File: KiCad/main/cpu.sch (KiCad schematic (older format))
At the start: 15 parts, among them SW1 SW_Push, U1 74HC245, U2 8284, U3 74HC245, U4 8086, U5 74HC573, U6 74HC573, U7 74HC573, Y1 30 MHz

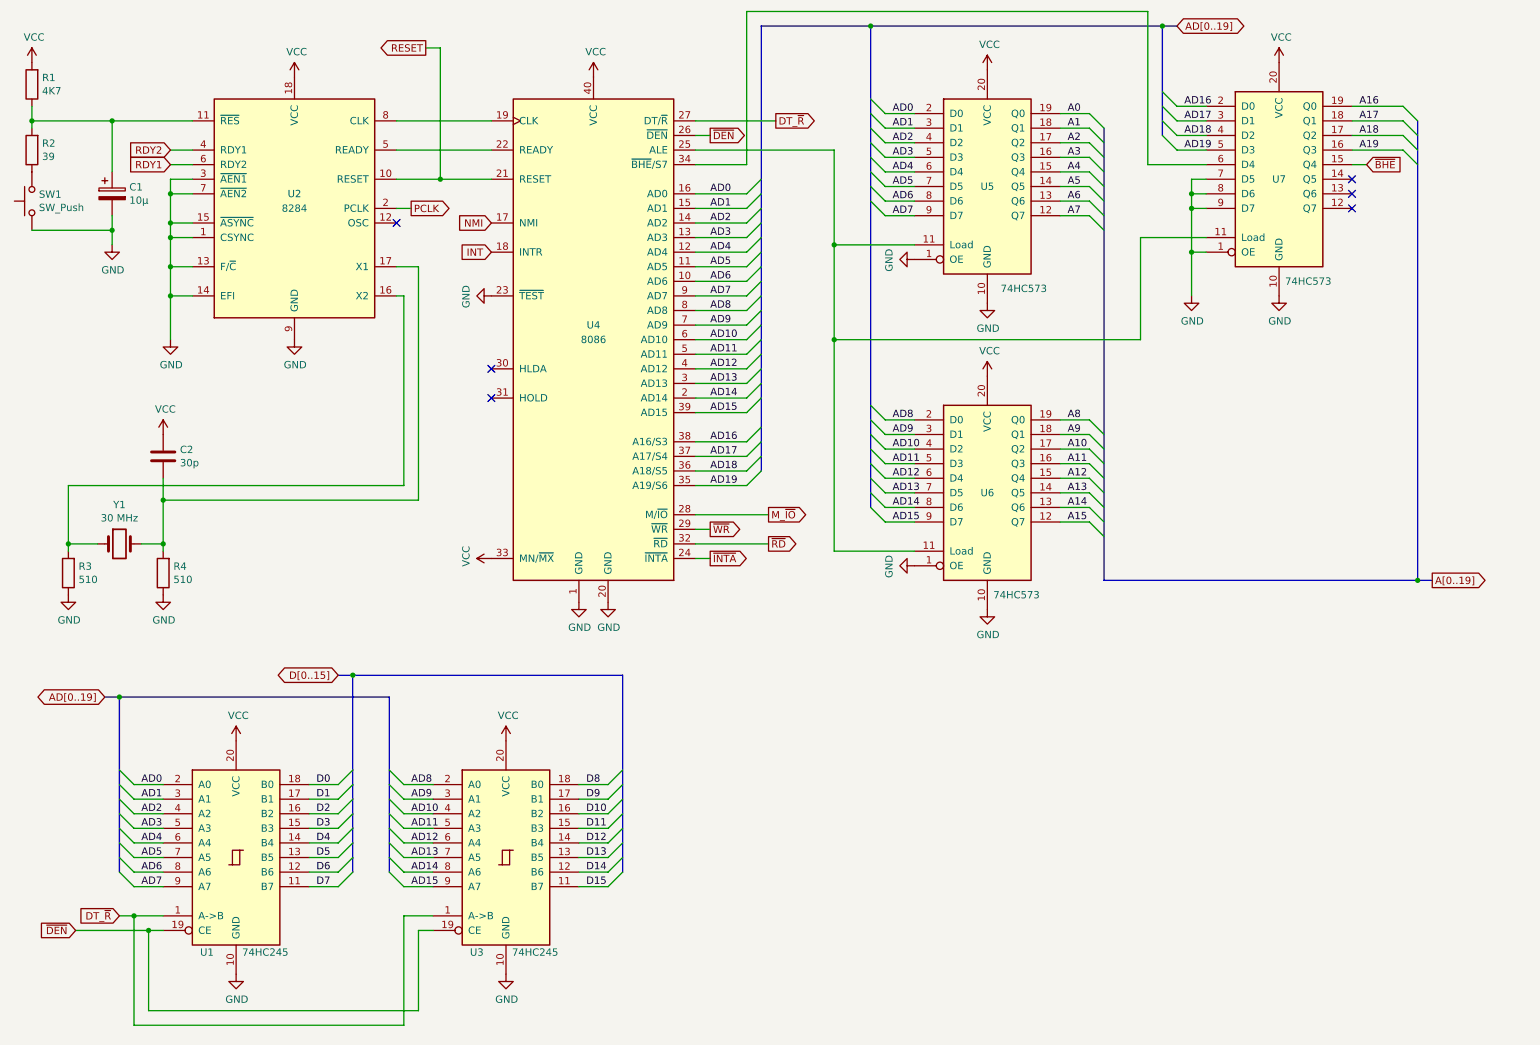
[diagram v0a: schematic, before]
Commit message: Updated graphics adapter and main schematics + board.
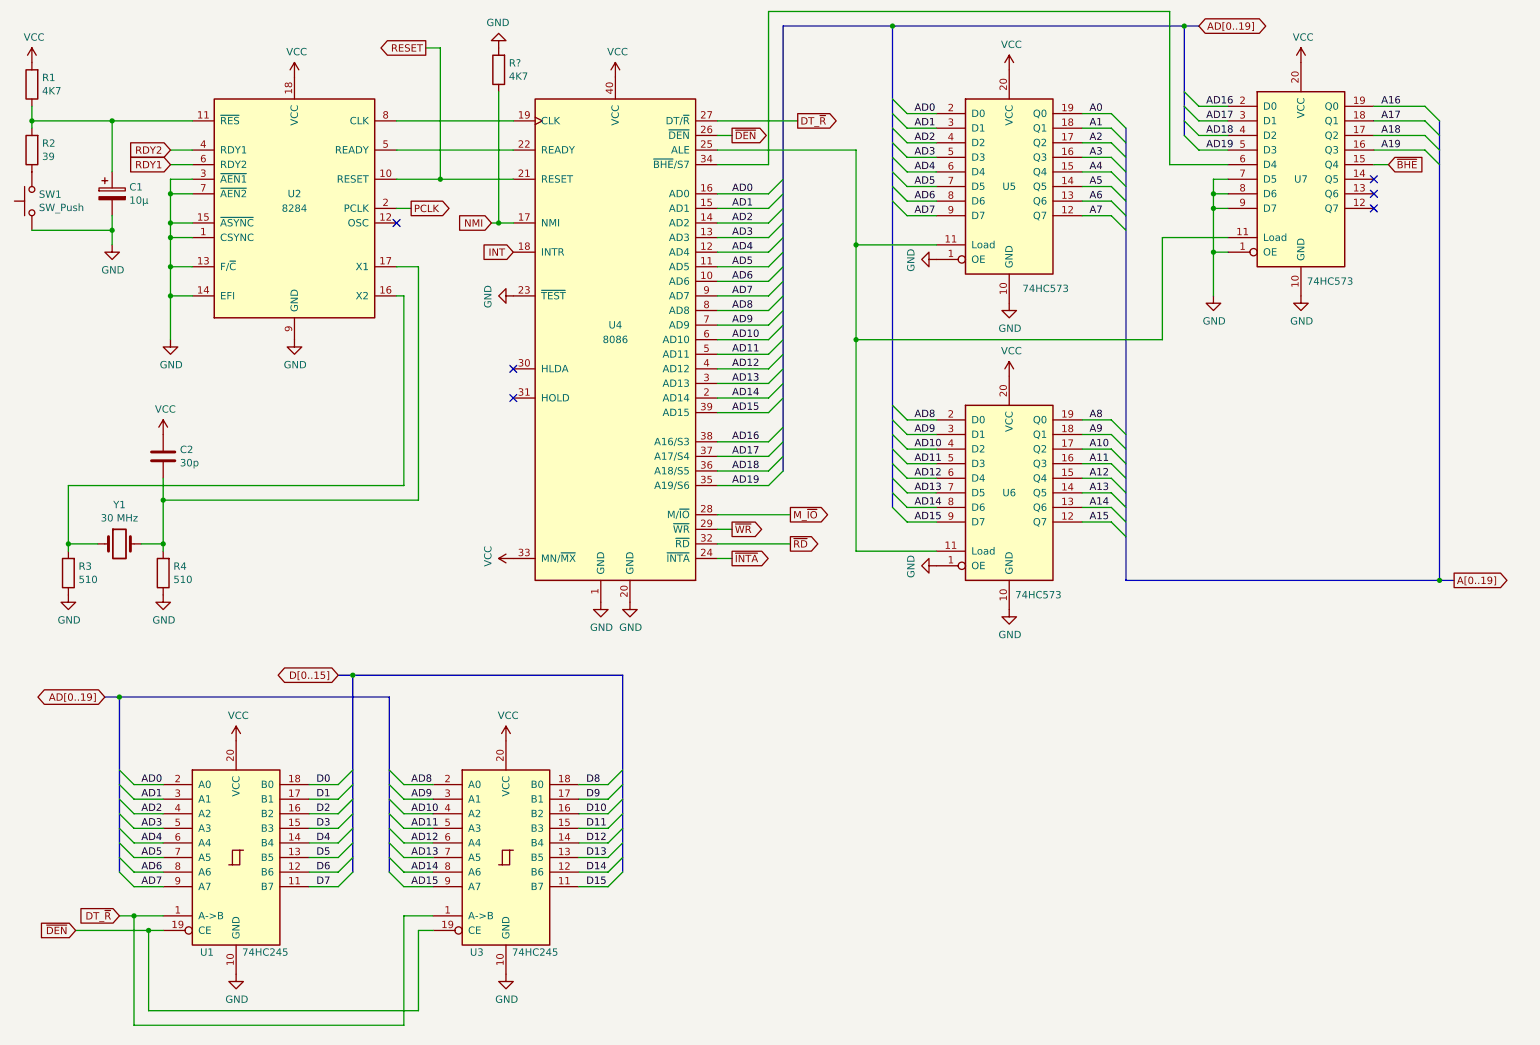
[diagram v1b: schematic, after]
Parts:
- added R?: 4K7, Resistor_THT:R_Axial_DIN0207_L6.3mm_D2.5mm_P7.62mm_Horizontal, symbol Device:R
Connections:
- net GND: now also R?.2
- net NMI: now also R?.1
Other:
- moved on the sheet: U4, U5, U6, U7

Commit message: Updated KiCad VGA board and main board.
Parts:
- added R7, R8: 4K7, Resistor_THT:R_Axial_DIN0207_L6.3mm_D2.5mm_P7.62mm_Horizontal, symbol Device:R
- gave numbers to parts that had none: 1
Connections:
- net GND: now also R7.1, R8.1; no longer U2.15 (~ASYNC~)
- net RDY1: now also R8.2
- net RDY2: now also R7.2
- no-connect marks 6 -> 8
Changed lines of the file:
@@
 	2050 1850 1900 1850
-Wire Wire Line
-	1900 1850 1900 2050
-Wire Wire Line
-	2050 2050 1900 2050
-Connection ~ 1900 2050
-Wire Wire Line
-	1900 2050 1900 2150
 Wire Wire Line
 	2050 1750 1900 1750
@@
 	4250 2050 4150 2050
 $Comp
-L Device:R R?
+L Device:R R6
 U 1 1 5F819246
 P 4150 1000
-F 0 "R?" H 4080 954 50  0000 R CNN
+F 0 "R6" H 4080 954 50  0000 R CNN
 F 1 "4K7" H 4080 1045 50  0000 R CNN
 F 2 "Resistor_THT:R_Axial_DIN0207_L6.3mm_D2.5mm_P7.62mm_Horizontal" V 4080 1000 50  0001 C CNN
@@
 	4150 2050 4100 2050
 $Comp
-L power:GND #PWR?
+L power:GND #PWR0102
 U 1 1 5F833B90
 P 4150 850
-F 0 "#PWR?" H 4150 600 50  0001 C CNN
+F 0 "#PWR0102" H 4150 600 50  0001 C CNN
 F 1 "GND" H 4155 677 50  0000 C CNN
 F 2 "" H 4150 850 50  0001 C CNN
@@
 	-1   0    0    1
 $EndComp
+Wire Wire Line
+	1900 1850 1900 2150
+NoConn ~ 2050 2050
+Text GLabel 5950 5450 1    50   Input ~ 0
+RDY2
+Text GLabel 6250 5450 1    50   Input ~ 0
+RDY1
+$Comp
+L Device:R R7
+U 1 1 5F82E30F
+P 5950 5700
+F 0 "R7" H 5880 5654 50  0000 R CNN
+F 1 "4K7" H 5880 5745 50  0000 R CNN
+F 2 "Resistor_THT:R_Axial_DIN0207_L6.3mm_D2.5mm_P7.62mm_Horizontal" V 5880 5700 50  0001 C CNN
+F 3 "~" H 5950 5700 50  0001 C CNN
+	1    5950 5700
+	-1   0    0    1
+$EndComp
+$Comp
+L power:GND #PWR056
+U 1 1 5F82EA67
+P 5950 6150
+F 0 "#PWR056" H 5950 5900 50  0001 C CNN
+F 1 "GND" H 5955 5977 50  0000 C CNN
+F 2 "" H 5950 6150 50  0001 C CNN
+F 3 "" H 5950 6150 50  0001 C CNN
+	1    5950 6150
+	1    0    0    -1
+$EndComp
+$Comp
+L Device:R R8
+U 1 1 5F82EE29
+P 6250 5700
+F 0 "R8" H 6180 5654 50  0000 R CNN
+F 1 "4K7" H 6180 5745 50  0000 R CNN
+F 2 "Resistor_THT:R_Axial_DIN0207_L6.3mm_D2.5mm_P7.62mm_Horizontal" V 6180 5700 50  0001 C CNN
+F 3 "~" H 6250 5700 50  0001 C CNN
+	1    6250 5700
+	-1   0    0    1
+$EndComp
+NoConn ~ 5150 4900
+Wire Wire Line
+	5950 5850 5950 6000
+Wire Wire Line
+	6250 5850 6250 6000
+Wire Wire Line
+	6250 6000 5950 6000
+Connection ~ 5950 6000
+Wire Wire Line
+	5950 6000 5950 6150
+Wire Wire Line
+	6250 5550 6250 5450
+Wire Wire Line
+	5950 5550 5950 5450
 Wire Bus Line
 	10600 1350 10600 4500

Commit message: Updated main system board schematics and board.
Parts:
- added U13: 74HC32, Package_DIP:DIP-14_W7.62mm_LongPads, symbol 74xx:74LS32
- added U15: 74HC08, Package_DIP:DIP-14_W7.62mm_LongPads, symbol 74xx:74LS08
- R7, R8: value 4K7 -> 10K
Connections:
- net A0: now also U15.1
- net GND: now also U15.10, U15.12, U15.13, U15.7 (GND), U15.9
- net RESET: now also U15.6; no longer U2.10 (RESET), U4.21 (RESET)
- net VCC: now also U15.14 (VCC)
- net ~BHE: now also U13.13
- net ~DEN: now also U13.12, U13.9; no longer U1.19 (CE), U3.19 (CE)
- net ~INTA: now also U15.2
- net CLK: now reaches U2.8 (CLK), U4.19 (CLK)
- net READY: now reaches U2.5 (READY), U4.22 (READY)
- net ALE: now reaches U4.25 (ALE), U5.11 (Load), U6.11 (Load), U7.11 (Load)
- net ~RES: now reaches C1.1, R1.1, R2.2, U2.11 (~RES~)
- new net: U13.10, U15.3
- new net CPU_RESET: U15.4, U15.5, U2.10 (RESET), U4.21 (RESET)
- new net ~CE_DHI: U13.11, U3.19 (CE)
- new net ~CE_DLO: U1.19 (CE), U13.8
- no-connect marks 8 -> 9
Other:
- moved on the sheet: R7, R8, U1, U3

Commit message: Fixed main and info_board bugs.
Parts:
- R7, R8: value 10K -> 4K7
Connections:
- net GND: now also U4.31 (HOLD); no longer R7.1, R8.1
- net VCC: now also R7.1, R8.1
- no-connect marks 9 -> 8
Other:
- moved on the sheet: R7, R8, U15C, U15D, U15E
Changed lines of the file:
@@
 A19
 Wire Wire Line
-	5200 7350 3350 7350
-NoConn ~ 4250 3250
+	5200 7350 3400 7350
 NoConn ~ 4250 3050
 NoConn ~ 3450 2050
-Text GLabel 1500 6700 0    50   Input ~ 0
+Text GLabel 1550 6700 0    50   Input ~ 0
 ~DEN
 Text GLabel 3250 6700 0    50   Input ~ 0
 DT_~R
-Connection ~ 3350 6700
-Wire Wire Line
-	3250 6700 3350 6700
-Wire Wire Line
-	3350 6700 3550 6700
-Wire Wire Line
-	3350 7350 3350 6700
+Connection ~ 3400 6700
+Wire Wire Line
+	3250 6700 3400 6700
+Wire Wire Line
+	3400 6700 3550 6700
+Wire Wire Line
+	3400 7350 3400 6700
 Wire Wire Line
 	5200 6700 5200 7350
@@
 	1900 1850 1900 2150
 NoConn ~ 2050 2050
-Text GLabel 9150 3250 1    50   Input ~ 0
+Text GLabel 9550 3950 3    50   Input ~ 0
 RDY2
-Text GLabel 9450 3250 1    50   Input ~ 0
+Text GLabel 9250 3950 3    50   Input ~ 0
 RDY1
 $Comp
 L Device:R R7
 U 1 1 5F82E30F
-P 9150 3500
-F 0 "R7" H 9080 3454 50  0000 R CNN
-F 1 "10K" H 9080 3545 50  0000 R CNN
-F 2 "Resistor_THT:R_Axial_DIN0207_L6.3mm_D2.5mm_P7.62mm_Horizontal" V 9080 3500 50  0001 C CNN
-F 3 "~" H 9150 3500 50  0001 C CNN
-	1    9150 3500
-	-1   0    0    1
-$EndComp
-$Comp
-L power:GND #PWR056
-U 1 1 5F82EA67
-P 9150 3950
-F 0 "#PWR056" H 9150 3700 50  0001 C CNN
-F 1 "GND" H 9155 3777 50  0000 C CNN
-F 2 "" H 9150 3950 50  0001 C CNN
-F 3 "" H 9150 3950 50  0001 C CNN
-	1    9150 3950
+P 9550 3700
+F 0 "R7" H 9480 3654 50  0000 R CNN
+F 1 "4K7" H 9480 3745 50  0000 R CNN
+F 2 "Resistor_THT:R_Axial_DIN0207_L6.3mm_D2.5mm_P7.62mm_Horizontal" V 9480 3700 50  0001 C CNN
+F 3 "~" H 9550 3700 50  0001 C CNN
+	1    9550 3700
 	1    0    0    -1
 $EndComp
@@
 L Device:R R8
 U 1 1 5F82EE29
-P 9450 3500
-F 0 "R8" H 9380 3454 50  0000 R CNN
-F 1 "10K" H 9380 3545 50  0000 R CNN
-F 2 "Resistor_THT:R_Axial_DIN0207_L6.3mm_D2.5mm_P7.62mm_Horizontal" V 9380 3500 50  0001 C CNN
-F 3 "~" H 9450 3500 50  0001 C CNN
-	1    9450 3500
-	-1   0    0    1
-$EndComp
-Wire Wire Line
-	9150 3650 9150 3800
-Wire Wire Line
-	9450 3650 9450 3800
-Wire Wire Line
-	9450 3800 9150 3800
-Connection ~ 9150 3800
-Wire Wire Line
-	9150 3800 9150 3950
-Wire Wire Line
-	9450 3350 9450 3250
-Wire Wire Line
-	9150 3350 9150 3250
+P 9250 3700
+F 0 "R8" H 9180 3654 50  0000 R CNN
+F 1 "4K7" H 9180 3745 50  0000 R CNN
+F 2 "Resistor_THT:R_Axial_DIN0207_L6.3mm_D2.5mm_P7.62mm_Horizontal" V 9180 3700 50  0001 C CNN
+F 3 "~" H 9250 3700 50  0001 C CNN
+	1    9250 3700
+	1    0    0    -1
+$EndComp
+Wire Wire Line
+	9550 3550 9550 3400
+Wire Wire Line
+	9250 3550 9250 3400
+Wire Wire Line
+	9250 3400 9550 3400
+Connection ~ 9550 3400
+Wire Wire Line
+	9550 3400 9550 3250
+Wire Wire Line
+	9250 3850 9250 3950
+Wire Wire Line
+	9550 3850 9550 3950
 Text Label 6250 1550 0    50   ~ 0
 ALE
@@
 ~CE_DHI
 Wire Wire Line
-	1500 6700 1700 6700
+	1550 6700 1700 6700
 Wire Wire Line
 	1850 7350 1700 7350
@@
 	1    0    0    -1
 $EndComp
-NoConn ~ 9350 5750
-NoConn ~ 9350 5100
-Wire Wire Line
-	8650 5000 8750 5000
-Wire Wire Line
-	8750 5200 8650 5200
-Connection ~ 8650 5200
-Wire Wire Line
-	8650 5200 8650 5000
-Wire Wire Line
-	8750 5850 8650 5850
-Wire Wire Line
-	8750 5650 8650 5650
-Connection ~ 8650 5650
-Wire Wire Line
-	8650 5650 8650 5200
-Wire Wire Line
-	8650 5650 8650 5850
-Connection ~ 8650 5850
+NoConn ~ 9350 5850
+NoConn ~ 9350 5200
+Wire Wire Line
+	8650 5100 8750 5100
+Wire Wire Line
+	8750 5300 8650 5300
+Connection ~ 8650 5300
+Wire Wire Line
+	8650 5300 8650 5100
+Wire Wire Line
+	8750 5950 8650 5950
+Wire Wire Line
+	8750 5750 8650 5750
+Connection ~ 8650 5750
+Wire Wire Line
+	8650 5750 8650 5300
+Wire Wire Line
+	8650 5750 8650 5950
+Connection ~ 8650 5950
 $Comp
 L power:GND #PWR0105
 U 1 1 5FA31EF9
-P 10100 6000
-F 0 "#PWR0105" H 10100 5750 50  0001 C CNN
-F 1 "GND" H 10105 5827 50  0000 C CNN
-F 2 "" H 10100 6000 50  0001 C CNN
-F 3 "" H 10100 6000 50  0001 C CNN
-	1    10100 6000
+P 10100 6100
+F 0 "#PWR0105" H 10100 5850 50  0001 C CNN
+F 1 "GND" H 10105 5927 50  0000 C CNN
+F 2 "" H 10100 6100 50  0001 C CNN
+F 3 "" H 10100 6100 50  0001 C CNN
+	1    10100 6100
 	1    0    0    -1
 $EndComp
@@
 L power:VCC #PWR0108
 U 1 1 5FA326F1
-P 10100 5000
-F 0 "#PWR0108" H 10100 4850 50  0001 C CNN
-F 1 "VCC" H 10115 5173 50  0000 C CNN
-F 2 "" H 10100 5000 50  0001 C CNN
-F 3 "" H 10100 5000 50  0001 C CNN
-	1    10100 5000
+P 10100 5100
+F 0 "#PWR0108" H 10100 4950 50  0001 C CNN
+F 1 "VCC" H 10115 5273 50  0000 C CNN
+F 2 "" H 10100 5100 50  0001 C CNN
+F 3 "" H 10100 5100 50  0001 C CNN
+	1    10100 5100
 	1    0    0    -1
 $EndComp
@@
 L 74xx:74LS08 U15
 U 3 1 5F933B11
-P 9050 5100
-F 0 "U15" H 9050 5425 50  0000 C CNN
-F 1 "74HC08" H 9050 5334 50  0000 C CNN
-F 2 "Package_DIP:DIP-14_W7.62mm_LongPads" H 9050 5100 50  0001 C CNN
-F 3 "http://www.ti.com/lit/gpn/sn74LS08" H 9050 5100 50  0001 C CNN
-	3    9050 5100
+P 9050 5200
+F 0 "U15" H 9050 5525 50  0000 C CNN
+F 1 "74HC08" H 9050 5434 50  0000 C CNN
+F 2 "Package_DIP:DIP-14_W7.62mm_LongPads" H 9050 5200 50  0001 C CNN
+F 3 "http://www.ti.com/lit/gpn/sn74LS08" H 9050 5200 50  0001 C CNN
+	3    9050 5200
 	1    0    0    -1
 $EndComp
@@
 L 74xx:74LS08 U15
 U 4 1 5F9359D8
-P 9050 5750
-F 0 "U15" H 9050 6075 50  0000 C CNN
-F 1 "74HC08" H 9050 5984 50  0000 C CNN
-F 2 "Package_DIP:DIP-14_W7.62mm_LongPads" H 9050 5750 50  0001 C CNN
-F 3 "http://www.ti.com/lit/gpn/sn74LS08" H 9050 5750 50  0001 C CNN
-	4    9050 5750
+P 9050 5850
+F 0 "U15" H 9050 6175 50  0000 C CNN
+F 1 "74HC08" H 9050 6084 50  0000 C CNN
+F 2 "Package_DIP:DIP-14_W7.62mm_LongPads" H 9050 5850 50  0001 C CNN
+F 3 "http://www.ti.com/lit/gpn/sn74LS08" H 9050 5850 50  0001 C CNN
+	4    9050 5850
 	1    0    0    -1
 $EndComp
@@
 L 74xx:74LS08 U15
 U 5 1 5F93755C
-P 10100 5500
-F 0 "U15" H 10330 5546 50  0000 L CNN
-F 1 "74HC08" H 10330 5455 50  0000 L CNN
-F 2 "Package_DIP:DIP-14_W7.62mm_LongPads" H 10100 5500 50  0001 C CNN
-F 3 "http://www.ti.com/lit/gpn/sn74LS08" H 10100 5500 50  0001 C CNN
-	5    10100 5500
-	1    0    0    -1
-$EndComp
-Wire Wire Line
-	8650 5850 8650 6100
+P 10100 5600
+F 0 "U15" H 10330 5646 50  0000 L CNN
+F 1 "74HC08" H 10330 5555 50  0000 L CNN
+F 2 "Package_DIP:DIP-14_W7.62mm_LongPads" H 10100 5600 50  0001 C CNN
+F 3 "http://www.ti.com/lit/gpn/sn74LS08" H 10100 5600 50  0001 C CNN
+	5    10100 5600
+	1    0    0    -1
+$EndComp
+Wire Wire Line
+	8650 5950 8650 6100
 Wire Wire Line
 	3450 1750 3850 1750
@@
 Wire Wire Line
 	3850 4250 3200 4250
+$Comp
+L power:GND #PWR?
+U 1 1 5FA5E367
+P 4250 3250
+F 0 "#PWR?" H 4250 3000 50  0001 C CNN
+F 1 "GND" H 4255 3077 50  0000 C CNN
+F 2 "" H 4250 3250 50  0001 C CNN
+F 3 "" H 4250 3250 50  0001 C CNN
+	1    4250 3250
+	0    1    1    0
+$EndComp
+$Comp
+L power:VCC #PWR?
+U 1 1 5FA8AF8C
+P 9550 3250
+F 0 "#PWR?" H 9550 3100 50  0001 C CNN
+F 1 "VCC" H 9565 3423 50  0000 C CNN
+F 2 "" H 9550 3250 50  0001 C CNN
+F 3 "" H 9550 3250 50  0001 C CNN
+	1    9550 3250
+	1    0    0    -1
+$EndComp
 Wire Bus Line
 	10600 1350 10600 4500

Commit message: Fixed CPU board bugs.
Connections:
- net GND: now also R7.1
- net VCC: no longer R7.1
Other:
- moved on the sheet: R7
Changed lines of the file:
@@
 	1900 1850 1900 2150
 NoConn ~ 2050 2050
-Text GLabel 9550 3950 3    50   Input ~ 0
+Text GLabel 9500 3400 1    50   Input ~ 0
 RDY2
 Text GLabel 9250 3950 3    50   Input ~ 0
@@
 L Device:R R7
 U 1 1 5F82E30F
-P 9550 3700
-F 0 "R7" H 9480 3654 50  0000 R CNN
-F 1 "4K7" H 9480 3745 50  0000 R CNN
-F 2 "Resistor_THT:R_Axial_DIN0207_L6.3mm_D2.5mm_P7.62mm_Horizontal" V 9480 3700 50  0001 C CNN
-F 3 "~" H 9550 3700 50  0001 C CNN
-	1    9550 3700
-	1    0    0    -1
+P 9500 3700
+F 0 "R7" H 9430 3654 50  0000 R CNN
+F 1 "4K7" H 9430 3745 50  0000 R CNN
+F 2 "Resistor_THT:R_Axial_DIN0207_L6.3mm_D2.5mm_P7.62mm_Horizontal" V 9430 3700 50  0001 C CNN
+F 3 "~" H 9500 3700 50  0001 C CNN
+	1    9500 3700
+	-1   0    0    1
 $EndComp
 $Comp
@@
 $EndComp
 Wire Wire Line
-	9550 3550 9550 3400
-Wire Wire Line
-	9250 3550 9250 3400
-Wire Wire Line
-	9250 3400 9550 3400
-Connection ~ 9550 3400
-Wire Wire Line
-	9550 3400 9550 3250
-Wire Wire Line
 	9250 3850 9250 3950
 Wire Wire Line
-	9550 3850 9550 3950
+	9500 3550 9500 3400
 Text Label 6250 1550 0    50   ~ 0
 ALE
@@
 L power:VCC #PWR?
 U 1 1 5FA8AF8C
-P 9550 3250
-F 0 "#PWR?" H 9550 3100 50  0001 C CNN
-F 1 "VCC" H 9565 3423 50  0000 C CNN
-F 2 "" H 9550 3250 50  0001 C CNN
-F 3 "" H 9550 3250 50  0001 C CNN
-	1    9550 3250
-	1    0    0    -1
-$EndComp
+P 9250 3250
+F 0 "#PWR?" H 9250 3100 50  0001 C CNN
+F 1 "VCC" H 9265 3423 50  0000 C CNN
+F 2 "" H 9250 3250 50  0001 C CNN
+F 3 "" H 9250 3250 50  0001 C CNN
+	1    9250 3250
+	1    0    0    -1
+$EndComp
+Wire Wire Line
+	9250 3250 9250 3550
+Wire Wire Line
+	9500 3850 9500 3950
 Wire Bus Line
 	10600 1350 10600 4500
@@
 Wire Bus Line
 	6100 700  6100 3750
+$Comp
+L power:GND #PWR?
+U 1 1 5FC8586F
+P 9500 3950
+F 0 "#PWR?" H 9500 3700 50  0001 C CNN
+F 1 "GND" H 9505 3777 50  0000 C CNN
+F 2 "" H 9500 3950 50  0001 C CNN
+F 3 "" H 9500 3950 50  0001 C CNN
+	1    9500 3950
+	1    0    0    -1
+$EndComp
 $EndSCHEMATC

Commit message: Updated CPU board
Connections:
- net ~BHE_S7: now reaches U4.34 (~BHE~/S7), U7.6 (D4)
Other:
- moved on the sheet: U15A
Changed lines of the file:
@@
 	1700 6700 1850 6700
 Wire Wire Line
-	1800 6100 2050 6100
+	1950 6100 2200 6100
 Wire Wire Line
 	1850 7550 1550 7550
@@
 ~BHE
 Entry Wire Line
-	2050 6100 2150 6200
-Wire Bus Line
-	2150 6200 2200 6200
-Text Label 1850 6100 0    50   ~ 0
+	2200 6100 2300 6200
+Wire Bus Line
+	2300 6200 2350 6200
+Text Label 2000 6100 0    50   ~ 0
 A0
-Text GLabel 2200 6200 2    50   Input ~ 0
+Text GLabel 2350 6200 2    50   Input ~ 0
 A[0..19]
 $Comp
@@
 	1000 6900 1000 6000
 Wire Wire Line
-	1000 6000 1200 6000
-Wire Wire Line
-	1800 5900 2200 5900
-Text GLabel 2200 5900 2    50   Input ~ 0
+	1000 6000 1350 6000
+Wire Wire Line
+	1950 5900 2350 5900
+Text GLabel 2350 5900 2    50   Input ~ 0
 ~INTA
 $Comp
 L 74xx:74LS08 U15
 U 1 1 5F92AC69
-P 1500 6000
-F 0 "U15" H 1500 5683 50  0000 C CNN
-F 1 "74HC08" H 1500 5774 50  0000 C CNN
-F 2 "Package_DIP:DIP-14_W7.62mm_LongPads" H 1500 6000 50  0001 C CNN
-F 3 "http://www.ti.com/lit/gpn/sn74LS08" H 1500 6000 50  0001 C CNN
-	1    1500 6000
+P 1650 6000
+F 0 "U15" H 1650 5683 50  0000 C CNN
+F 1 "74HC08" H 1650 5774 50  0000 C CNN
+F 2 "Package_DIP:DIP-14_W7.62mm_LongPads" H 1650 6000 50  0001 C CNN
+F 3 "http://www.ti.com/lit/gpn/sn74LS08" H 1650 6000 50  0001 C CNN
+	1    1650 6000
 	-1   0    0    1
 $EndComp
@@
 Wire Wire Line
 	9500 3850 9500 3950
-Wire Bus Line
-	10600 1350 10600 4500
-Wire Bus Line
-	8850 700  8850 1450
-Wire Bus Line
-	6700 5050 6700 6400
-Wire Bus Line
-	4850 5050 4850 6400
-Wire Bus Line
-	5100 5200 5100 6400
-Wire Bus Line
-	3250 5200 3250 6400
-Wire Bus Line
-	8450 1400 8450 4500
-Wire Bus Line
-	6850 700  6850 4000
-Wire Bus Line
-	6100 700  6100 3750
 $Comp
 L power:GND #PWR?
@@
 	1    0    0    -1
 $EndComp
+Text Label 5700 1650 0    50   ~ 0
+~BHE_S7
+Wire Bus Line
+	10600 1350 10600 4500
+Wire Bus Line
+	8850 700  8850 1450
+Wire Bus Line
+	6700 5050 6700 6400
+Wire Bus Line
+	4850 5050 4850 6400
+Wire Bus Line
+	5100 5200 5100 6400
+Wire Bus Line
+	3250 5200 3250 6400
+Wire Bus Line
+	8450 1400 8450 4500
+Wire Bus Line
+	6850 700  6850 4000
+Wire Bus Line
+	6100 700  6100 3750
 $EndSCHEMATC
